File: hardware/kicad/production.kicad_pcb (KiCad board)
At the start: 2 copper layers, 136.8 x 86 mm, 41 parts

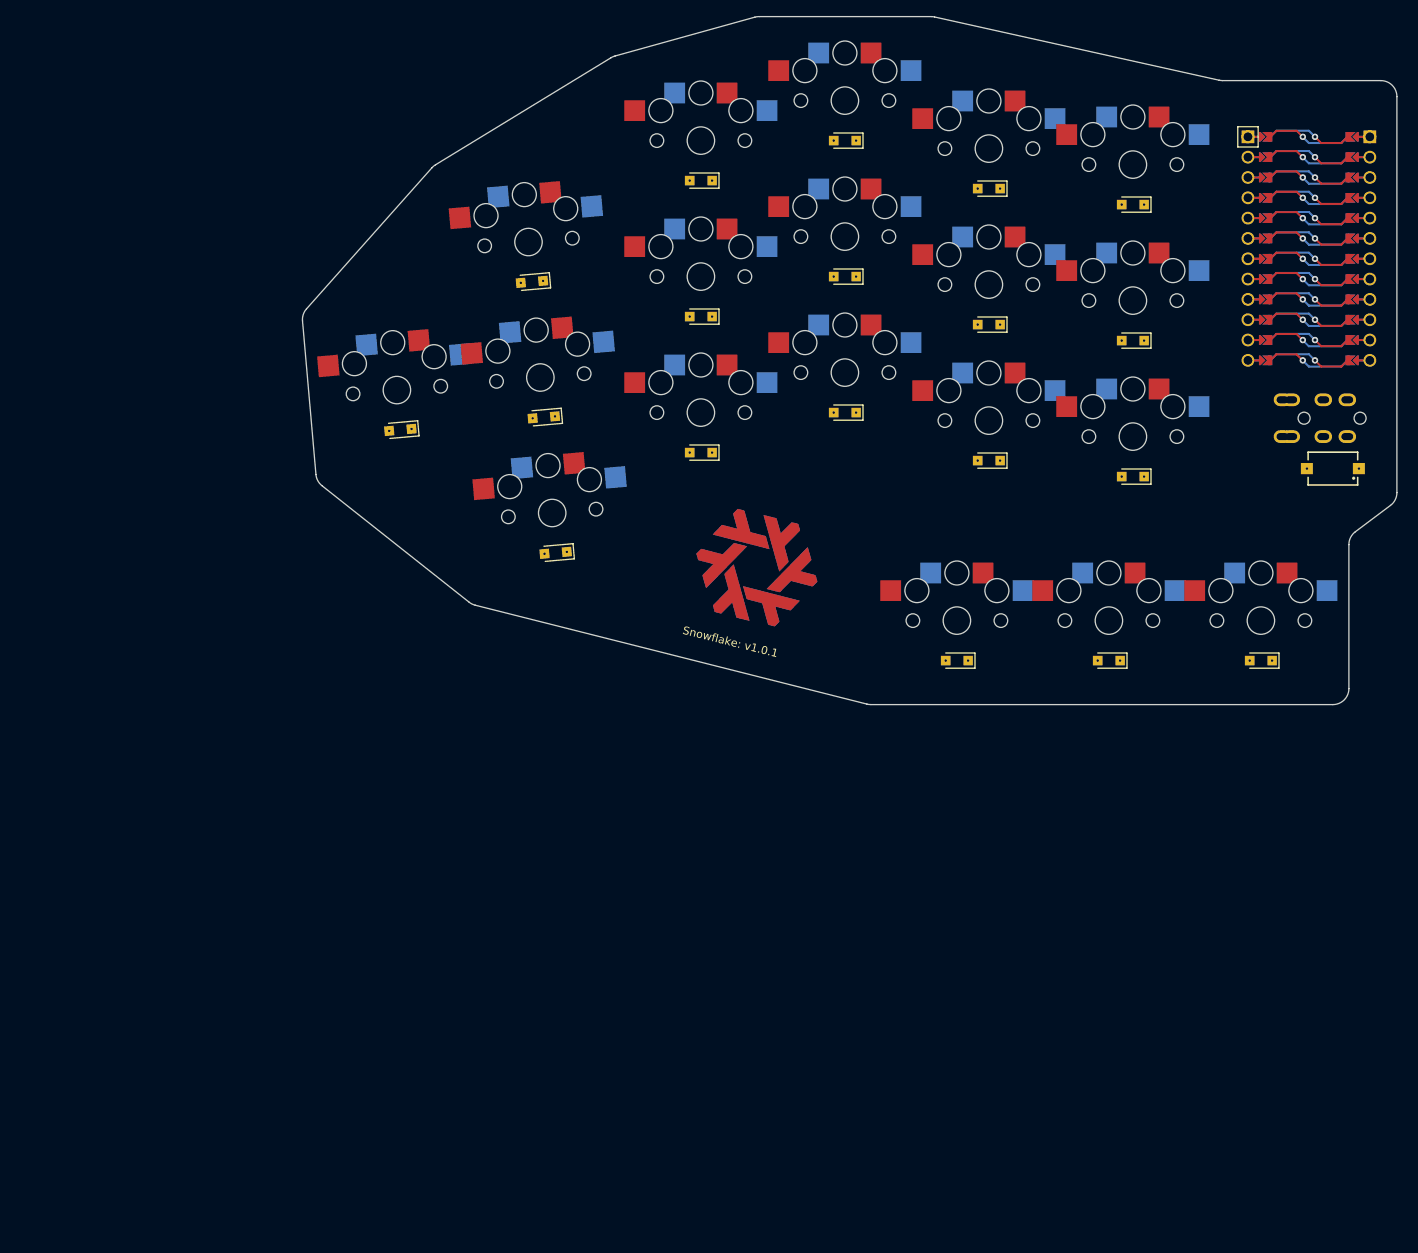
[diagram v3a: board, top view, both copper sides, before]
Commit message: wired the keyboard
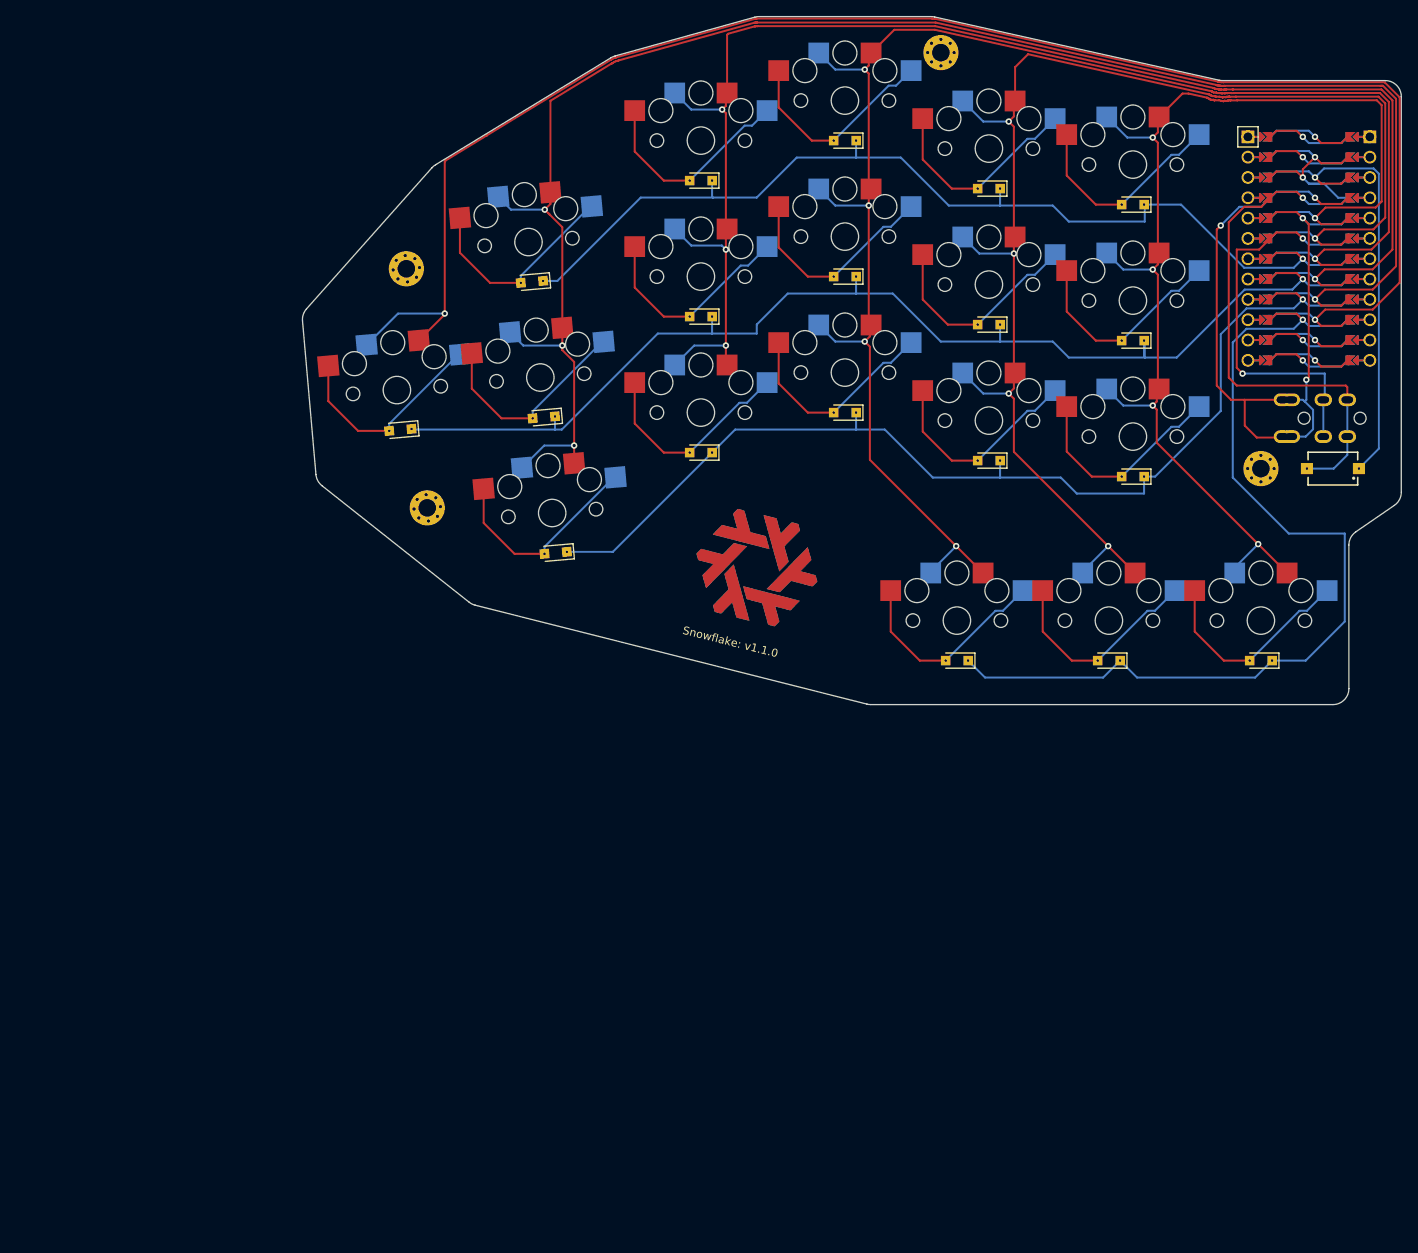
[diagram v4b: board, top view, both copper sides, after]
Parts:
- added _1: , MountingHole_2.2mm_M2_Pad_Via, F.Cu at (166.5, 40.9)
- added _2: , MountingHole_2.2mm_M2_Pad_Via, F.Cu at (206.5, 92.9)
- added _3: , MountingHole_2.2mm_M2_Pad_Via, F.Cu at (99.7, 67.9)
- added _4: , MountingHole_2.2mm_M2_Pad_Via, F.Cu at (102.3, 97.8)
- D1, D10, D11, D12, D13, D14, D15, D16, D17, D18, D19, D2, D3, D4, D5, D6, D7, D8, D9: moved to F.Cu
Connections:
- D1 pad 1: P0 -> P5
- D10 pad 1: P1 -> P4
- D11 pad 1: P4 -> P6
- D12 pad 1: P0 -> P5
- D13 pad 1: P1 -> P4
- D14 pad 1: P4 -> P6
- D15 pad 1: P0 -> P5
- D16 pad 1: P1 -> P4
- D17 pad 1: P5 -> P7
- D18 pad 1: P5 -> P7
- D19 pad 1: P5 -> P7
- D2 pad 1: P4 -> P6
- D3 pad 1: P0 -> P5
- D4 pad 1: P1 -> P4
- D5 pad 1: P4 -> P6
- D6 pad 1: P0 -> P5
- D7 pad 1: P1 -> P4
- D8 pad 1: P4 -> P6
- D9 pad 1: P0 -> P5
- S1 pad 1: P6 -> P14
- S10 pad 1: P9 -> P19
- S11 pad 1: P21 -> P20
- S12 pad 1: P21 -> P20
- S13 pad 1: P21 -> P20
- S14 pad 1: P20 -> P21
- S15 pad 1: P20 -> P21
- S16 pad 1: P20 -> P21
- S17 pad 1: P9 -> P19
- S18 pad 1: P21 -> P20
- S19 pad 1: P20 -> P21
- S2 pad 1: P7 -> P15
- S3 pad 1: P7 -> P15
- S4 pad 1: P7 -> P15
- S5 pad 1: P8 -> P18
- S6 pad 1: P8 -> P18
- S7 pad 1: P8 -> P18
- S8 pad 1: P9 -> P19
- S9 pad 1: P9 -> P19
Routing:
- net (no net): track 262.1 -> 0.00 mm
- net P15: track 0.00 -> 222.0 mm, vias 1 -> 4
- net P14: track 0.00 -> 207.1 mm, vias 1 -> 2
- net P19: track 0.00 -> 202.6 mm, vias 1 -> 5
- net P18: track 0.00 -> 189.2 mm, vias 1 -> 4
- net P20: track 0.00 -> 179.5 mm, vias 1 -> 5
- net P21: track 0.00 -> 152.2 mm, vias 1 -> 5
- net P5: track 0.00 -> 149.6 mm
- net P6: track 0.00 -> 133.7 mm
- net P4: track 0.00 -> 127.9 mm
- net P7: track 0.00 -> 118.3 mm
- net GND: track 0.00 -> 96.9 mm
- net RST: track 0.00 -> 57.5 mm
- net VCC: track 0.00 -> 55.7 mm, vias 1 -> 2
- net P3: track 0.00 -> 49.7 mm, vias 1 -> 2
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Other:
- board size 136.8 x 86 mm -> 137.4 x 86 mm
- net class Default removed
- board text added: "Snowflake: v1.1.0"
- board text removed: "Snowflake: v1.0.1"
